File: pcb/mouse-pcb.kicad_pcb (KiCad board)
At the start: 4 copper layers, 89.5 x 71.4 mm, 47 parts, among them J1 TYPE-C-31-M-12, SW1 D2FC-F-7N20M, SW2 D2FC-F-7N20M, SW3 D2FC-F-7N20M, U1 PAW3395-T6QU, U2 NRF52840-QIAA-R7, Y1 32MHz, Y2 32.768kHz

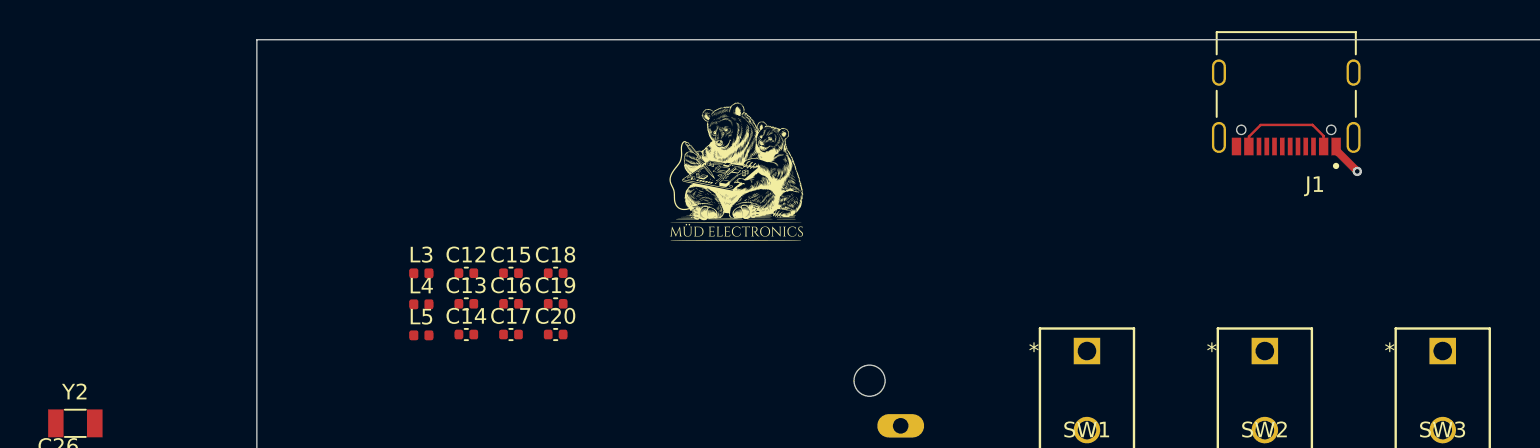
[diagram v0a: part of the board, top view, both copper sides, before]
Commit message: feat: usblc6 added
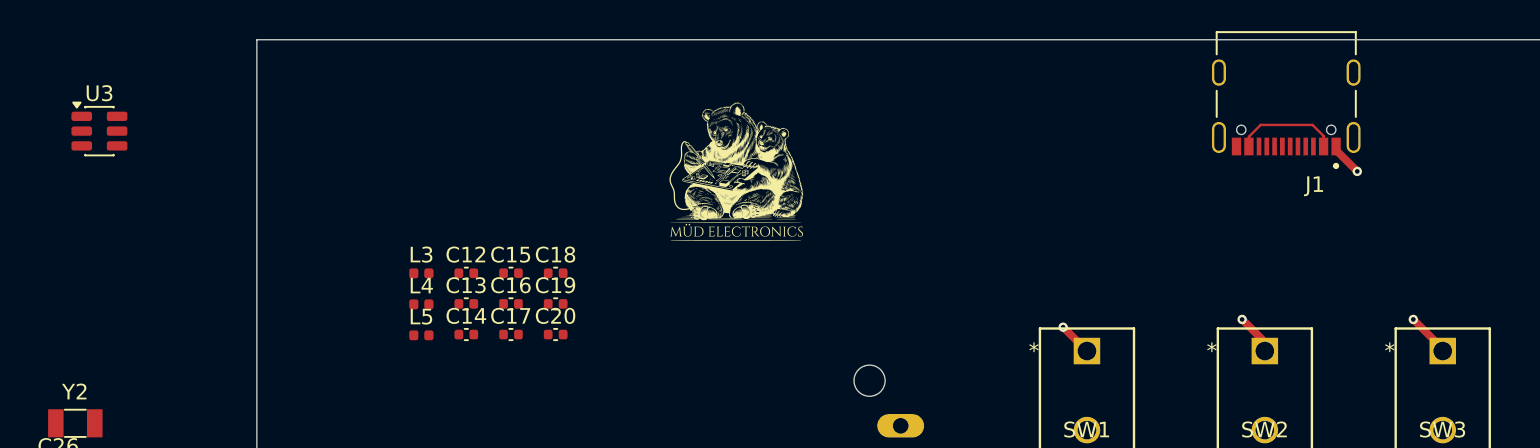
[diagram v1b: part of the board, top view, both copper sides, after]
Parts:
- added U3: USBLC6-2SC6, Package_TO_SOT_SMD:SOT-23-6, F.Cu at (49.6, 35.4)
- SW1: value D2FC-F-7N20M -> left click
- SW2: value D2FC-F-7N20M -> center click
- SW3: value D2FC-F-7N20M -> right click
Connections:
- SW1 pad 1: unconnected-(SW1-COM-Pad1) -> +3V3
- SW1 pad 2: unconnected-(SW1-NO-Pad2) -> LCLIKC
- SW2 pad 1: unconnected-(SW2-COM-Pad1) -> +3V3
- SW2 pad 2: unconnected-(SW2-NO-Pad2) -> CCLICK
- SW3 pad 1: unconnected-(SW3-COM-Pad1) -> +3V3
- SW3 pad 2: unconnected-(SW3-NO-Pad2) -> RCLICK
- U2 pad AD18: unconnected-(U2A-P0.22-PadAD18) -> RCLICK
- U2 pad AD20: unconnected-(U2A-P0.24-PadAD20) -> CCLICK
- U2 pad AD22: unconnected-(U2A-P1.00-PadAD22) -> LCLIKC
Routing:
- net +3V3: track 9.74 -> 17.4 mm, vias 2 -> 5

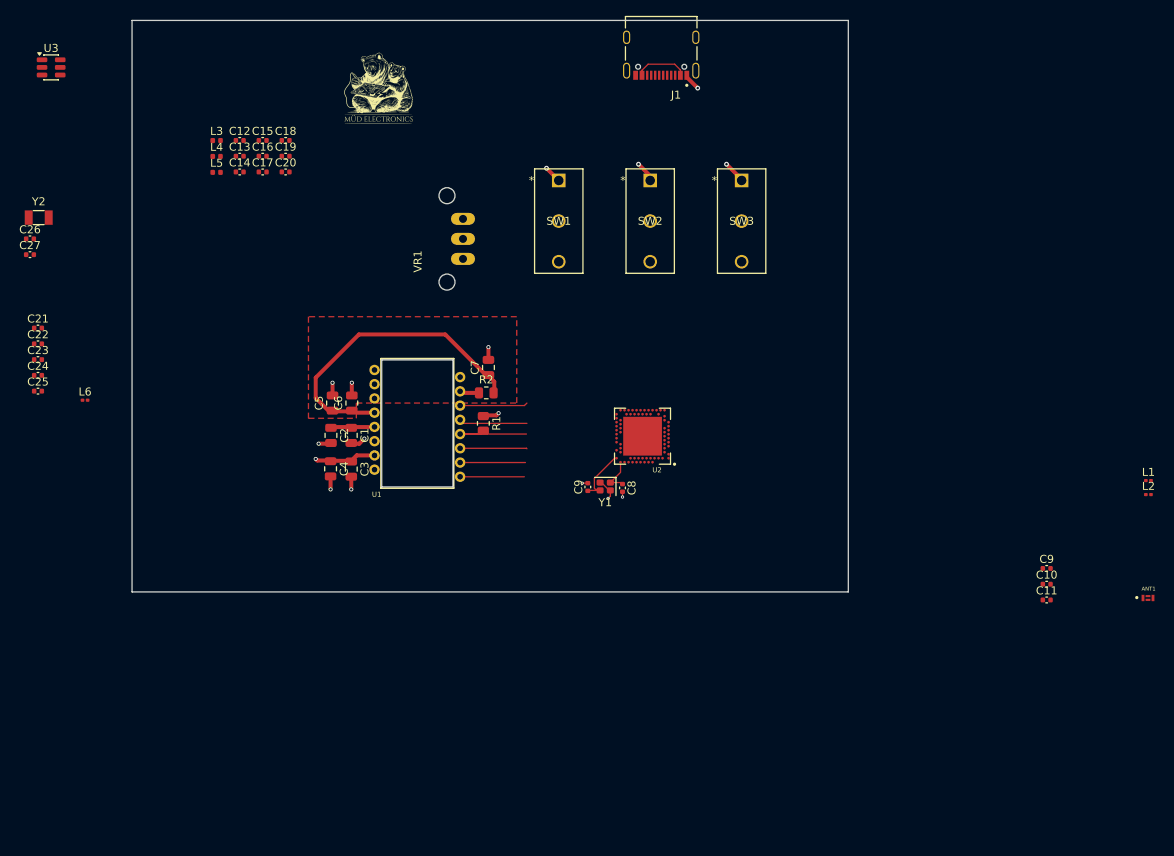
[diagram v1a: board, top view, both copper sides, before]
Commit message: feat: battery management added, mcu circuits are ready
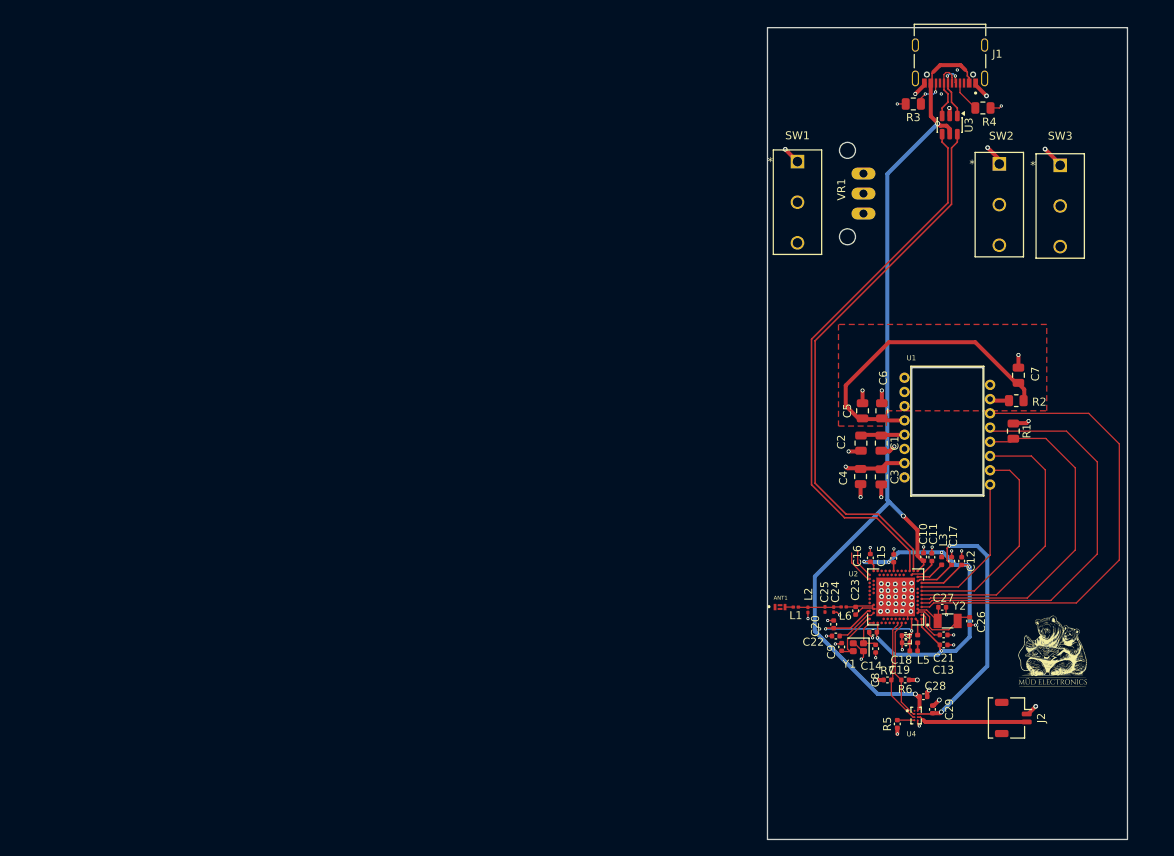
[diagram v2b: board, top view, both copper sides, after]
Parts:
- removed the C9 at (116.7, 87.8)
- removed the C9 at (174.0, 98.0)
- added C28: 1.0uF, Capacitor_SMD:C_0402_1005Metric, F.Cu at (158.6, 114.1)
- added C29: 10uF, Capacitor_SMD:C_0402_1005Metric, F.Cu at (159.7, 115.6)
- added C9: 12pF, Capacitor_SMD:C_0402_1005Metric, F.Cu at (148.4, 107.8)
- added J2: Conn_01x02, Connector_JST:JST_SHL_SM02B-SHLS-TF_1x02-1MP_P1.00mm_Horizontal, F.Cu at (169.8, 116.7)
- added R3: 5.1K, Capacitor_SMD:C_0805_2012Metric, F.Cu at (157.3, 40.0)
- added R4: 5.1K, Capacitor_SMD:C_0805_2012Metric, F.Cu at (166.1, 40.5)
- added R5: 10K, Capacitor_SMD:C_0402_1005Metric, F.Cu at (155.3, 117.5)
- added R6: 4.7K, Capacitor_SMD:C_0402_1005Metric, F.Cu at (156.3, 112.0)
- added R7: 4.7K, Capacitor_SMD:C_0402_1005Metric, F.Cu at (154.1, 112.0)
- added U4: BQ25180YBGR, mouse_library:IC_BQ25180YBGR, F.Cu at (157.7, 116.4)
- C24, C25: footprint Capacitor_SMD:C_0402_1005Metric -> Capacitor_SMD:C_0201_0603Metric
- R1: footprint Resistor_SMD:R_0805_2012Metric -> Capacitor_SMD:C_0805_2012Metric
- moved C26 126.8 mm to (164.4, 104.6), turned to 90 degrees
- moved Y2 124.3 mm to (161.6, 104.6)
- moved C27 122.2 mm to (161.0, 102.9)
- moved C21 119.5 mm to (161.1, 106.3), turned to 180 degrees
- moved U3 112.6 mm to (161.9, 42.6), turned to -90 degrees
- moved G*** 109.8 mm to (174.8, 108.4)
- moved C13 107.1 mm to (161.1, 107.6), turned to 180 degrees
- moved C23 106.9 mm to (150.1, 103.3), turned to 90 degrees
- moved L4 106.4 mm to (157.9, 106.8), turned to 90 degrees
- moved C22 106.2 mm to (147.7, 106.5)
- moved L5 105.7 mm to (157.4, 108.3)
- moved L3 104.8 mm to (160.9, 97.1), turned to -90 degrees
- moved C12 104.4 mm to (163.4, 97.1), turned to -90 degrees
- moved C24 103.7 mm to (147.4, 103.2), turned to 90 degrees
- moved C25 102.1 mm to (146.3, 103.2), turned to 90 degrees
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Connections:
- J1 pad A5: unconnected-(J1-CC1-PadA5) -> Net-(J1-CC1)
- J1 pad A6: unconnected-(J1-DP1-PadA6) -> USB D+
- J1 pad A7: unconnected-(J1-DN1-PadA7) -> USB D-
- J1 pad B5: unconnected-(J1-CC2-PadB5) -> Net-(J1-CC2)
- J1 pad B6: unconnected-(J1-DP2-PadB6) -> USB D+
- J1 pad B7: unconnected-(J1-DN2-PadB7) -> USB D-
- J1 pad S1: Net-(J1-SHIELD-PadS1) -> GND
- J1 pad S2: Net-(J1-SHIELD-PadS1) -> GND
- J1 pad S3: Net-(J1-SHIELD-PadS1) -> GND
- J1 pad S4: Net-(J1-SHIELD-PadS1) -> GND
- U2 pad A10: unconnected-(U2A-P0.29/AIN5-PadA10) -> SCL
- U2 pad A12: unconnected-(U2A-P0.02/AIN0-PadA12) -> SDA
- U2 pad G1: unconnected-(U2A-P0.26-PadG1) -> NRESET
- U2 pad J1: unconnected-(U2A-P0.04/AIN2-PadJ1) -> NCS
- U2 pad J24: MOTION -> unconnected-(U2A-P0.10/NFC2-PadJ24)
- U2 pad L1: unconnected-(U2A-P0.06-PadL1) -> MISO
- U2 pad L24: SCLK -> unconnected-(U2A-P0.09/NFC1-PadL24)
- U2 pad N1: unconnected-(U2A-P0.08-PadN1) -> MOSI
- U2 pad R1: NCS -> SCLK
- U2 pad R24: MOSI -> unconnected-(U2A-P1.06-PadR24)
- U2 pad U1: unconnected-(U2A-P0.12-PadU1) -> MOTION
- U2 pad U24: MISO -> unconnected-(U2A-P1.04-PadU24)
- U2 pad W24: NRESET -> unconnected-(U2A-P1.02-PadW24)
- U3 pad 1: unconnected-(U3-I/O1-Pad1) -> USB D-
- U3 pad 2: unconnected-(U3-GND-Pad2) -> GND
- U3 pad 3: unconnected-(U3-I/O2-Pad3) -> USB D+
- U3 pad 4: unconnected-(U3-I/O2-Pad4) -> D+
- U3 pad 5: unconnected-(U3-VBUS-Pad5) -> VBUS
- U3 pad 6: unconnected-(U3-I/O1-Pad6) -> D-
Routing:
- net VBUS: track 6.71 -> 115.6 mm, vias 0 -> 3
- net D-: track 0.00 -> 69.4 mm
- net D+: track 0.00 -> 69.4 mm
- net VDD: track 0.00 -> 54.9 mm, vias 0 -> 6
- net NRESET: track 8.48 -> 59.4 mm
- net NCS: track 8.53 -> 51.2 mm
- net VDDH: track 0.00 -> 38.0 mm, vias 0 -> 2
- net GND: track 17.1 -> 50.8 mm, vias 11 -> 64
- net MISO: track 11.3 -> 44.3 mm
- net MOSI: track 8.37 -> 35.1 mm
- net DEC4: track 0.00 -> 21.2 mm, vias 0 -> 2
- net SCLK: track 8.16 -> 26.9 mm
- net VBAT: track 0.00 -> 13.9 mm
- net SDA: track 0.00 -> 13.4 mm
- net SCL: track 0.00 -> 12.8 mm
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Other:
- board size 89.5 x 71.4 mm -> 45 x 101.5 mm
